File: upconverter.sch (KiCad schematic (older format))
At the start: 35 parts, among them J1 Barrel_Jack, J2 SMA_F, J3 SMA_F, U1 L7805, U2 TPS71533__SC70, U3 SA602A, X1 XO32

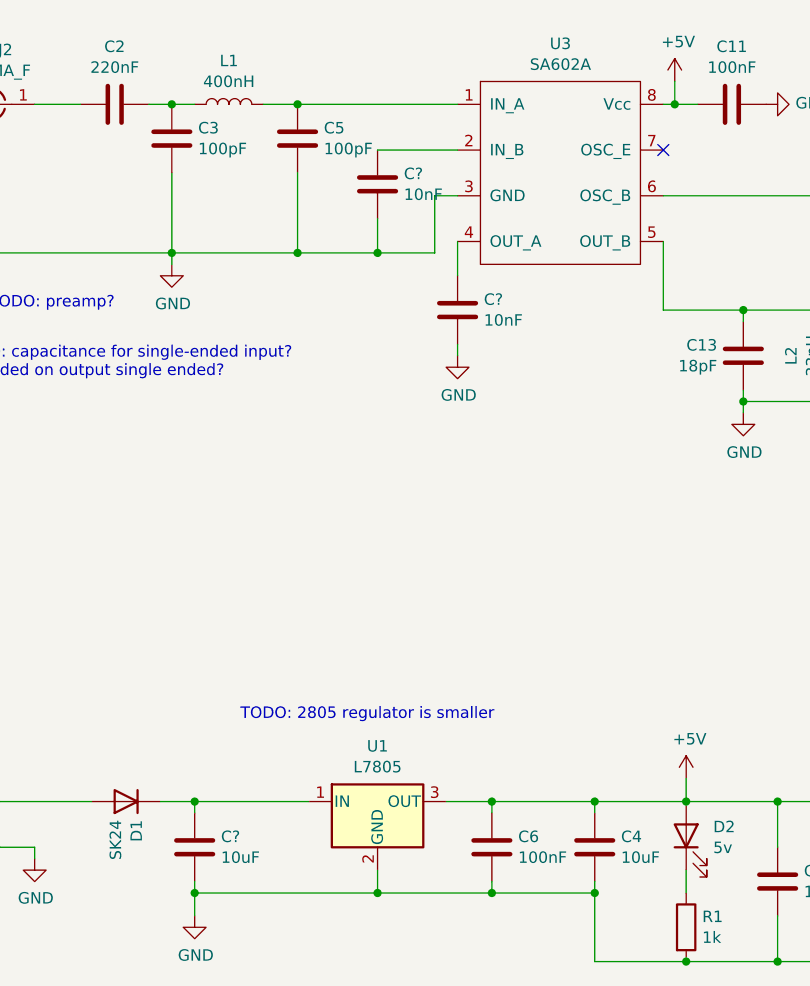
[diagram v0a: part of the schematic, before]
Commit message: Layout for single ended vers. TODO:needs silk screen text, fix ref des, lay tracks/fills, board size, TESTTT
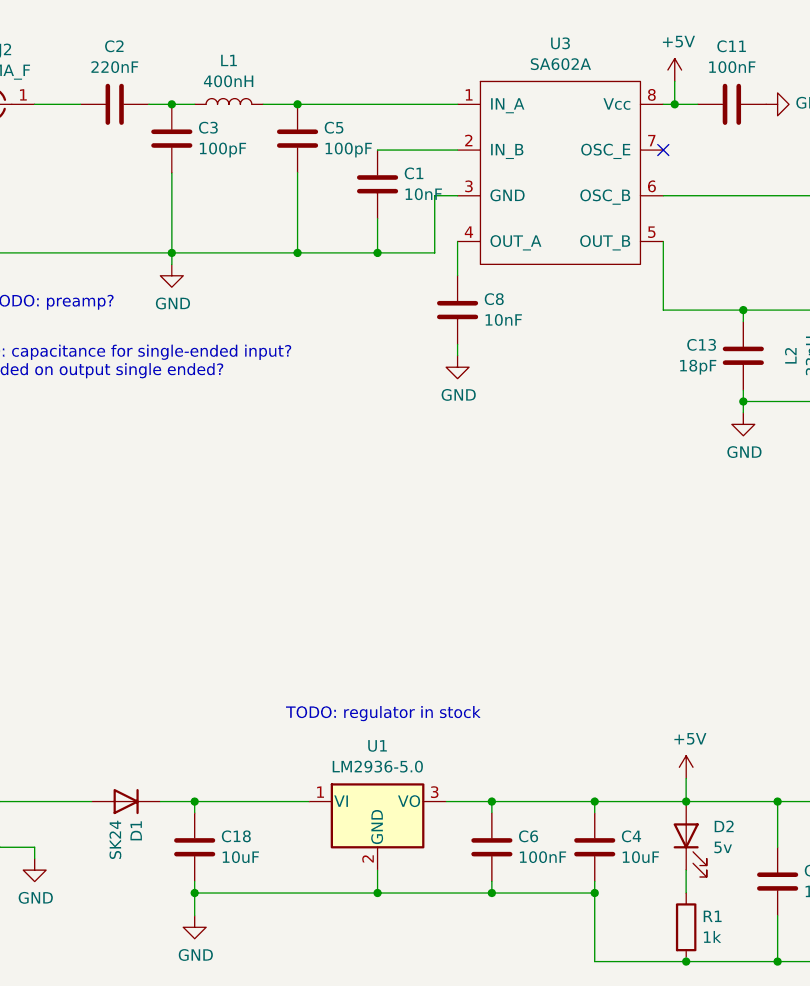
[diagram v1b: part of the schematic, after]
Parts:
- removed U1: L7805, Package_TO_SOT_THT:TO-220-3_Vertical, symbol Regulator_Linear:L7805
- added U1: LM2936-5.0, Package_TO_SOT_SMD:SOT-89-3, symbol Regulator_Linear:LM2936-5.0
- gave numbers to parts that had none: 3
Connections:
- net +5V: now also U1.3 (VO)
- net GND: now also U1.2 (GND)
- net at C18.1, D1.1 (K): now also U1.1 (VI)
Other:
- note added: "TODO: regulator in stock"
- note removed: "TODO: 2805 regulator is smaller"
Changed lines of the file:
@@
 Wire Wire Line
 	6800 7400 6800 7300
-$Comp
-L Regulator_Linear:L7805 U1
-U 1 1 60FC23BE
-P 7600 6900
-F 0 "U1" H 7600 7142 50  0000 C CNN
-F 1 "L7805" H 7600 7051 50  0000 C CNN
-F 2 "Package_TO_SOT_THT:TO-220-3_Vertical" H 7625 6750 50  0001 L CIN
-F 3 "http://www.st.com/content/ccc/resource/technical/document/datasheet/41/4f/b3/b0/12/d4/47/88/CD00000444.pdf/files/CD00000444.pdf/jcr:content/translations/en.CD00000444.pdf" H 7600 6850 50  0001 C CNN
-	1    7600 6900
-	1    0    0    -1
-$EndComp
 Wire Wire Line
 	7300 6900 6800 6900
@@
 	7250 3850 7950 3850
 $Comp
-L power:GND #PWR?
+L power:GND #PWR0101
 U 1 1 61166CB9
 P 6700 4550
-F 0 "#PWR?" H 6700 4300 50  0001 C CNN
+F 0 "#PWR0101" H 6700 4300 50  0001 C CNN
 F 1 "GND" H 6705 4377 50  0000 C CNN
 F 2 "" H 6700 4550 50  0001 C CNN
@@
 $EndComp
 $Comp
-L Device:C C?
+L Device:C C1
 U 1 1 61177755
 P 7600 4200
-F 0 "C?" H 7715 4246 50  0000 L CNN
+F 0 "C1" H 7715 4246 50  0000 L CNN
 F 1 "10nF" H 7715 4155 50  0000 L CNN
 F 2 "Capacitor_SMD:C_0603_1608Metric" H 7638 4050 50  0001 C CNN
@@
 TODO: capacitance for single-ended input?\nC needed on output single ended?
 $Comp
-L power:GND #PWR?
+L power:GND #PWR0102
 U 1 1 611B2FF2
 P 7950 4950
-F 0 "#PWR?" H 7950 4700 50  0001 C CNN
+F 0 "#PWR0102" H 7950 4700 50  0001 C CNN
 F 1 "GND" H 7955 4777 50  0000 C CNN
 F 2 "" H 7950 4950 50  0001 C CNN
@@
 $EndComp
 $Comp
-L Device:C C?
+L Device:C C8
 U 1 1 611B7EF2
 P 7950 4750
-F 0 "C?" H 8065 4796 50  0000 L CNN
+F 0 "C8" H 8065 4796 50  0000 L CNN
 F 1 "10nF" H 8065 4705 50  0000 L CNN
 F 2 "Capacitor_SMD:C_0603_1608Metric" H 7988 4600 50  0001 C CNN
@@
 	8850 4750 9200 4750
 $Comp
-L power:GND #PWR?
+L power:GND #PWR0103
 U 1 1 611F83C6
 P 9200 5200
-F 0 "#PWR?" H 9200 4950 50  0001 C CNN
+F 0 "#PWR0103" H 9200 4950 50  0001 C CNN
 F 1 "GND" H 9205 5027 50  0000 C CNN
 F 2 "" H 9200 5200 50  0001 C CNN
@@
 Wire Wire Line
 	9200 5200 9200 5150
-Text Notes 7000 6550 0    50   ~ 0
-TODO: 2805 regulator is smaller
 Text Notes 4350 4000 0    50   ~ 0
 TODO: Order parts dangit. Need the SMA\n
 $Comp
-L Device:C C?
+L Device:C C18
 U 1 1 6122E6E8
 P 6800 7100
-F 0 "C?" H 6915 7146 50  0000 L CNN
+F 0 "C18" H 6915 7146 50  0000 L CNN
 F 1 "10uF" H 6915 7055 50  0000 L CNN
 F 2 "Capacitor_SMD:C_0805_2012Metric" H 6838 6950 50  0001 C CNN
@@
 Wire Wire Line
 	8100 7300 8550 7300
+$Comp
+L Regulator_Linear:LM2936-5.0 U1
+U 1 1 61262CA5
+P 7600 6900
+F 0 "U1" H 7600 7142 50  0000 C CNN
+F 1 "LM2936-5.0" H 7600 7051 50  0000 C CNN
+F 2 "Package_TO_SOT_SMD:SOT-89-3" H 7600 7125 50  0001 C CIN
+F 3 "http://www.ti.com/lit/ds/symlink/lm2936.pdf" H 7600 6850 50  0001 C CNN
+	1    7600 6900
+	1    0    0    -1
+$EndComp
+Text Notes 7200 6550 0    50   ~ 0
+TODO: regulator in stock
 $EndSCHEMATC
